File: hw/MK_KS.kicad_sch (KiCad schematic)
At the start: 64 parts, among them J1 USB_OTG, J10 Screw_Terminal_01x02, J3 MKOB-Serial, J4 KEY_SND_IF, J8 Conn_Coaxial_Power, J9 Screw_Terminal_01x02, Q1 2N3904, Q1 G01N20LE, Q8 2N3905, SW1 CLOSER-SW, SW1 DASH-SW, SW1 KEY/DOT-SW, U1 MCP1702T-3302E, U3 LM358, U4 LM393ADR, U5 Sounder

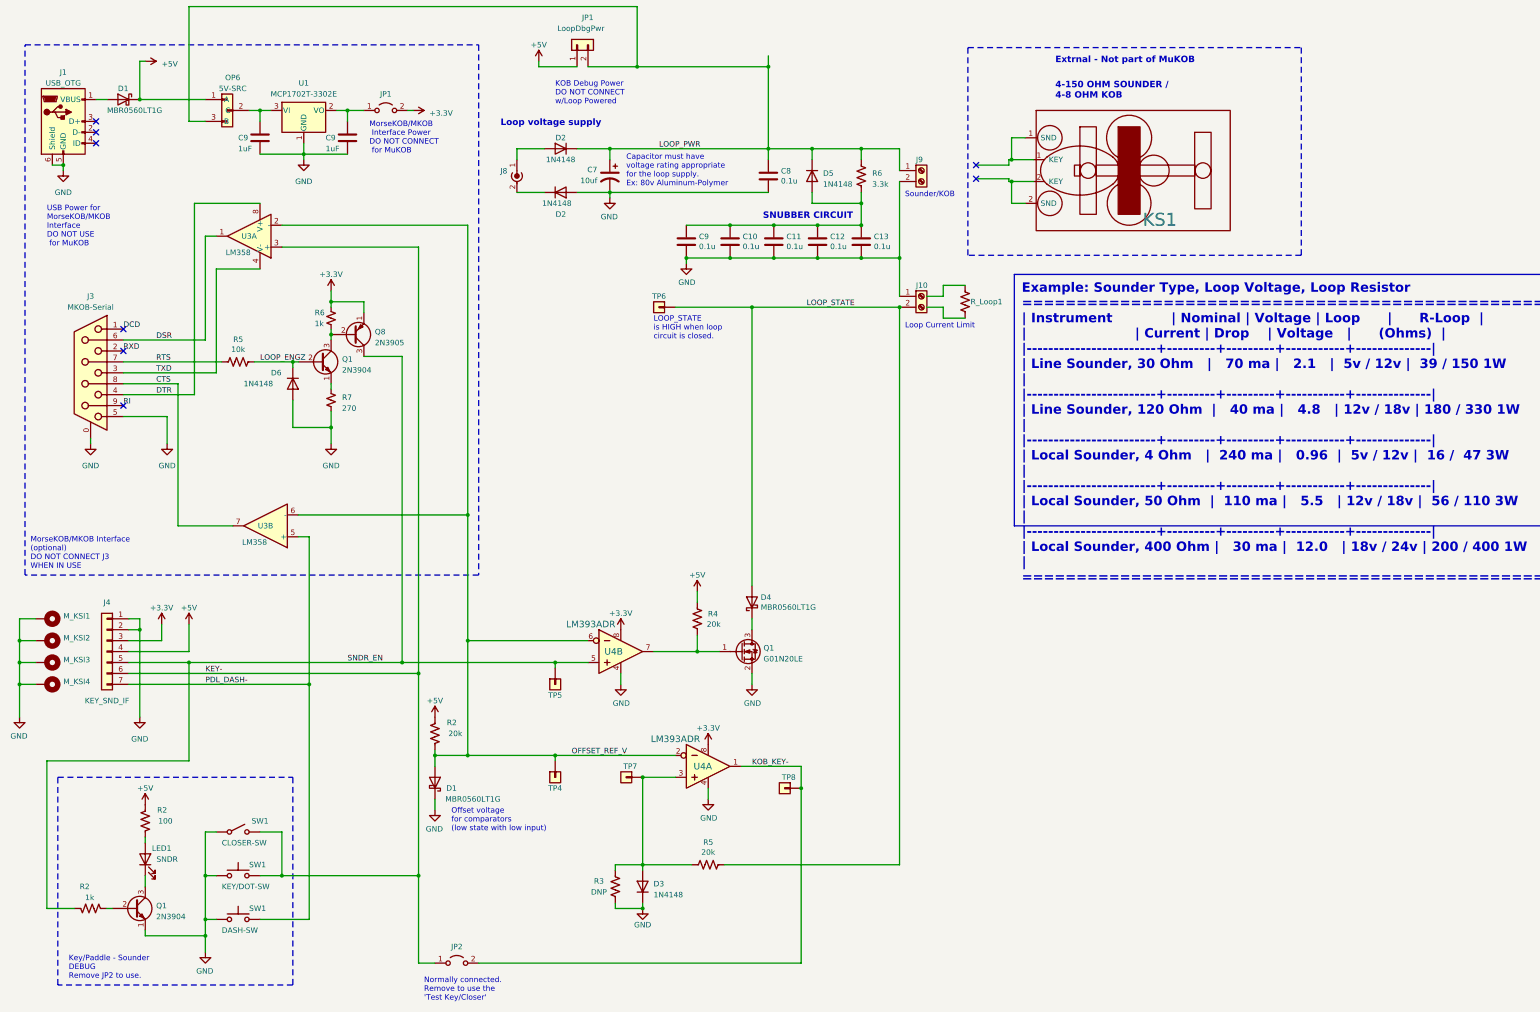
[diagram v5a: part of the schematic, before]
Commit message: Device (Main) and K&S-IF ready for layout.
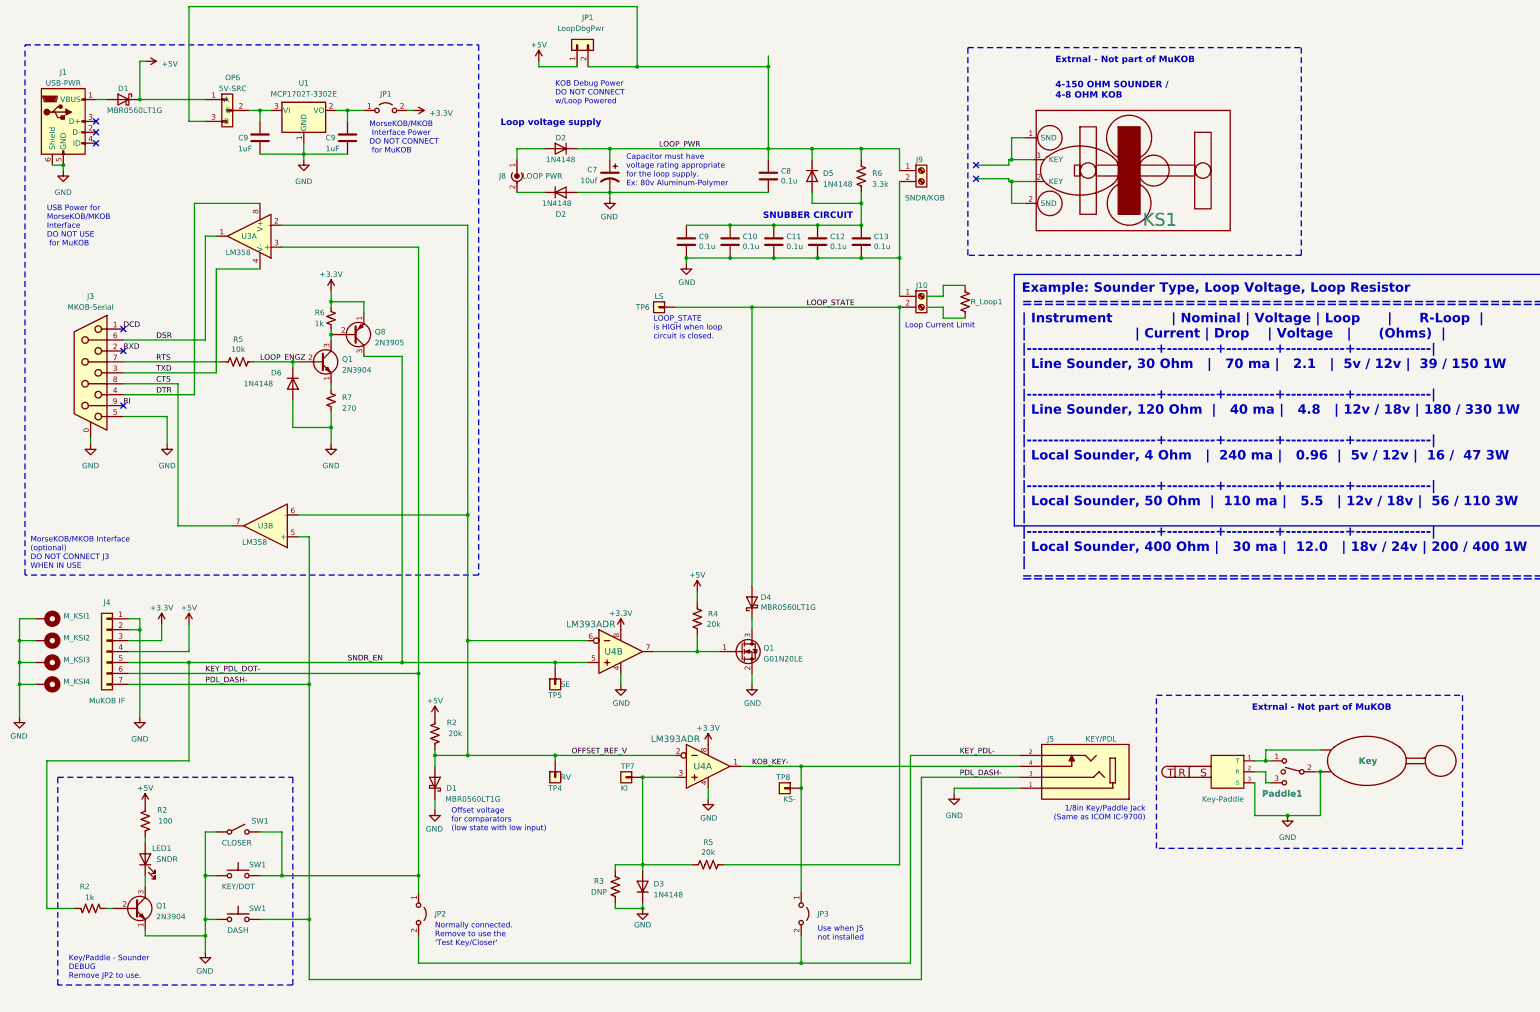
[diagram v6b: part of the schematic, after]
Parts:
- added J-SP1: Key-Paddle, symbol Audio-Plug-TRS:SP-TRS
- added J5: KEY/PDL, AES_Library:CUI_SJ1-3534NG-audio-jack, symbol AES_Library:CUI_SJ1-3534NG-audio-jack
- added JP3: 1x2 Header, Connector_PinHeader_2.54mm:PinHeader_1x02_P2.54mm_Vertical, symbol Jumper:Jumper_2_Open
- added KEY-EXT1: Key, symbol rpikobhat-rescue:Key-Telegraph
- added Paddle1: PDL_EXT, symbol Switch:SW_SPDT_MSM
- C10, C11, C12, C13, C8, C9: footprint Capacitor_SMD:C_1206_3216Metric_Pad1.33x1.80mm_HandSolder -> Capacitor_SMD:C_0603_1608Metric_Pad1.08x0.95mm_HandSolder
- C9: footprint Capacitor_SMD:C_1206_3216Metric_Pad1.33x1.80mm_HandSolder -> Capacitor_SMD:C_0201_0603Metric_Pad0.64x0.40mm_HandSolder
- J1: value USB_OTG -> USB-PWR
- J10: value Screw_Terminal_01x02 -> LOOP RES
- J4: value KEY_SND_IF -> MuKOB IF
- J8: value Conn_Coaxial_Power -> LOOP PWR
- J9: value Screw_Terminal_01x02 -> SNDR/KOB
- JP2: value 1x2 Header -> KEY-IN
- LED1: footprint LED_THT:LED_D5.0mm -> AES_Library:LED_SMD_SIDEVIEW_Harvatek
- R2, R3, R4, R5, R6: footprint Resistor_SMD:R_1206_3216Metric_Pad1.30x1.75mm_HandSolder -> Resistor_SMD:R_0402_1005Metric_Pad0.72x0.64mm_HandSolder
- R6, R7: footprint Resistor_THT:R_Axial_DIN0207_L6.3mm_D2.5mm_P10.16mm_Horizontal -> Resistor_SMD:R_0402_1005Metric_Pad0.72x0.64mm_HandSolder
- R_Loop1: footprint Resistor_SMD:R_1206_3216Metric_Pad1.30x1.75mm_HandSolder -> (none)
- SW1: value KEY/DOT-SW -> KEY/DOT; footprint Button_Switch_SMD:SW_Push_1P1T_NO_Vertical_Wuerth_434133025816 -> AES_Library:SW_PUSH_SMD_1P1T_NO_6x6mm
- SW1: value CLOSER-SW -> CLOSER
- SW1: value DASH-SW -> DASH; footprint Button_Switch_SMD:SW_Push_1P1T_NO_Vertical_Wuerth_434133025816 -> AES_Library:SW_PUSH_SMD_1P1T_NO_6x6mm
- TP4: value Test_Point_01 -> RV
- TP5: value Test_Point_01 -> SE
- TP6: value Test_Point_01 -> LS
- TP7: value Test_Point_01 -> KI
- TP8: value Test_Point_01 -> KS-
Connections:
- net GND: now also J-SP1.3 (S), J5.1, KEY-EXT1.2 (KEY), Paddle1.2
- net KOB_KEY-: now also J5.4, JP3.1 (A); no longer JP2.2 (B)
- net PDL_DASH-: now also J5.3
- net KEY- renamed KEY_PDL_DOT-
- new net: J-SP1.1 (T), KEY-EXT1.1 (KEY), Paddle1.1
- new net: J-SP1.2 (R), Paddle1.3
- new net KEY_PDL-: J5.2, JP2.2 (B), JP3.2 (B)
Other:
- note added: "1/8in Key/Paddle Jack (Same as ICOM IC-9700)"
- note added: "Use when J5 not installed"
- note removed: "Sounder/KOB"

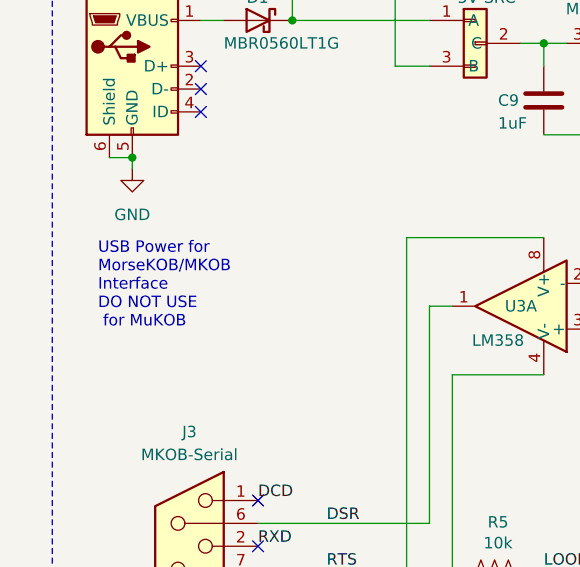
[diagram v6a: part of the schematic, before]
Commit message: Main PCB v1.0 complete.
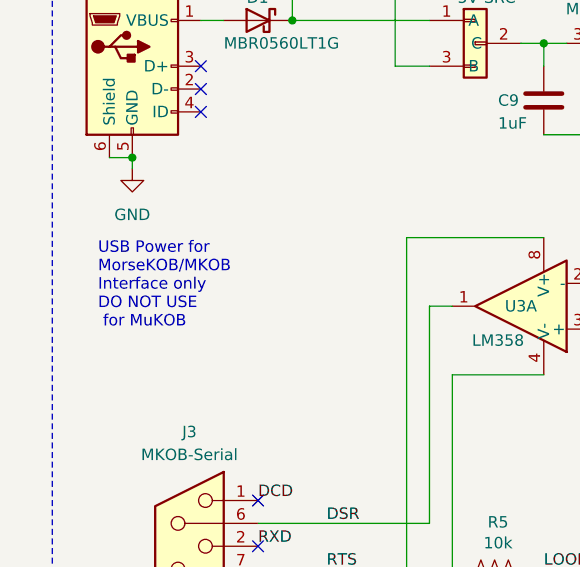
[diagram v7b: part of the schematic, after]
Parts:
- M_KSI1, M_KSI2, M_KSI3, M_KSI4: footprint MountingHole:MountingHole_3.2mm_M3_ISO7380 -> MountingHole:MountingHole_3.2mm_M3_ISO7380_Pad_TopBottom
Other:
- note added: "USB Power for MorseKOB/MKOB Interface only DO NOT USE for MuKOB"
- note removed: "USB Power for MorseKOB/MKOB Interface DO NOT USE for MuKOB"
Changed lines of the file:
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@@
     (effects (font (size 1.27 1.27)) (justify left bottom))
   )
-  (text "USB Power for\nMorseKOB/MKOB\nInterface\nDO NOT USE\n for MuKOB"
+  (text "USB Power for\nMorseKOB/MKOB\nInterface only\nDO NOT USE\n for MuKOB"
     (at 29.21 77.47 0)
     (effects (font (size 1.27 1.27)) (justify left bottom))
@@
       (effects (font (size 1.27 1.27)) (justify left) hide)
     )
-    (property "Footprint" "MountingHole:MountingHole_3.2mm_M3_ISO7380" (at 29.21 163.83 0)
+    (property "Footprint" "MountingHole:MountingHole_3.2mm_M3_ISO7380_Pad_TopBottom" (at 29.21 163.83 0)
       (effects (font (size 1.27 1.27)) hide)
     )
@@
       (effects (font (size 1.27 1.27)) (justify left) hide)
     )
-    (property "Footprint" "MountingHole:MountingHole_3.2mm_M3_ISO7380" (at 29.21 173.99 0)
+    (property "Footprint" "MountingHole:MountingHole_3.2mm_M3_ISO7380_Pad_TopBottom" (at 29.21 173.99 0)
       (effects (font (size 1.27 1.27)) hide)
     )
@@
       (effects (font (size 1.27 1.27)) (justify left) hide)
     )
-    (property "Footprint" "MountingHole:MountingHole_3.2mm_M3_ISO7380" (at 29.21 179.07 0)
+    (property "Footprint" "MountingHole:MountingHole_3.2mm_M3_ISO7380_Pad_TopBottom" (at 29.21 179.07 0)
       (effects (font (size 1.27 1.27)) hide)
     )
@@
       (effects (font (size 1.27 1.27)) (justify left) hide)
     )
-    (property "Footprint" "MountingHole:MountingHole_3.2mm_M3_ISO7380" (at 29.21 168.91 0)
-      (effects (font (size 1.27 1.27)) hide)
-    )
+    (property "Footprint" "MountingHole:MountingHole_3.2mm_M3_ISO7380_Pad_TopBottom" (at 29.21 168.91 0)
+      (effects (font (size 1.27 1.27)) hide)
+    )

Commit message: Add 3D components for rendering.
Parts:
- D2: footprint Diode_SMD:D_SOD-123 -> Diode_THT:D_DO-35_SOD27_P7.62mm_Horizontal
- J4: footprint Connector_PinSocket_2.54mm:PinSocket_1x07_P2.54mm_Vertical -> Connector_PinHeader_2.54mm:PinHeader_1x07_P2.54mm_Vertical
- J8: footprint Connector_BarrelJack:BarrelJack_CUI_PJ-036AH-SMT_Horizontal -> AES_Library:CUI_PJ-037B
- TP6: value LS -> LP2
- TP7: value KI -> LS
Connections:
- net LOOP_STATE: now also D3.2 (A), R3.2, R5.2, TP7.1 (Pin_1), U4.3; no longer D4.2 (A), J10.2 (Pin_2), R5.1, TP6.1 (Pin_1)
- net SNDR_EN-: now reaches Q1.1 (G), R4.1, U4.7 (2OUT)
- net LPI+: now reaches D2.2 (A), J8.1 (In)
- net LPI-: now reaches D2.1 (K), J8.2 (Ext)
- net V33RO: now reaches C9.1, JP1.1 (A), U1.2 (VO)
- net V33RI: now reaches C9.1, OP6.2 (C), U1.3 (VI)
- net V5I: now reaches D1.2 (A), J1.1 (VBUS)
- new net LP2: D4.2 (A), J10.2 (Pin_2), R5.1, TP6.1 (Pin_1)
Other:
- moved on the sheet: D1, R4, TP4
